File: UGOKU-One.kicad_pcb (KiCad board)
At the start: 2 copper layers, 70 x 70 mm, 80 parts, among them J1 ENC/IO, J10 Conn_01x02, J12 Conn_01x02, J2 SERVO, J3 Conn_02x03_Odd_Even, J4 14110213001000, J5 Conn_01x05, J6 Conn_01x02, J7 ENC/IO, J8 DAC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

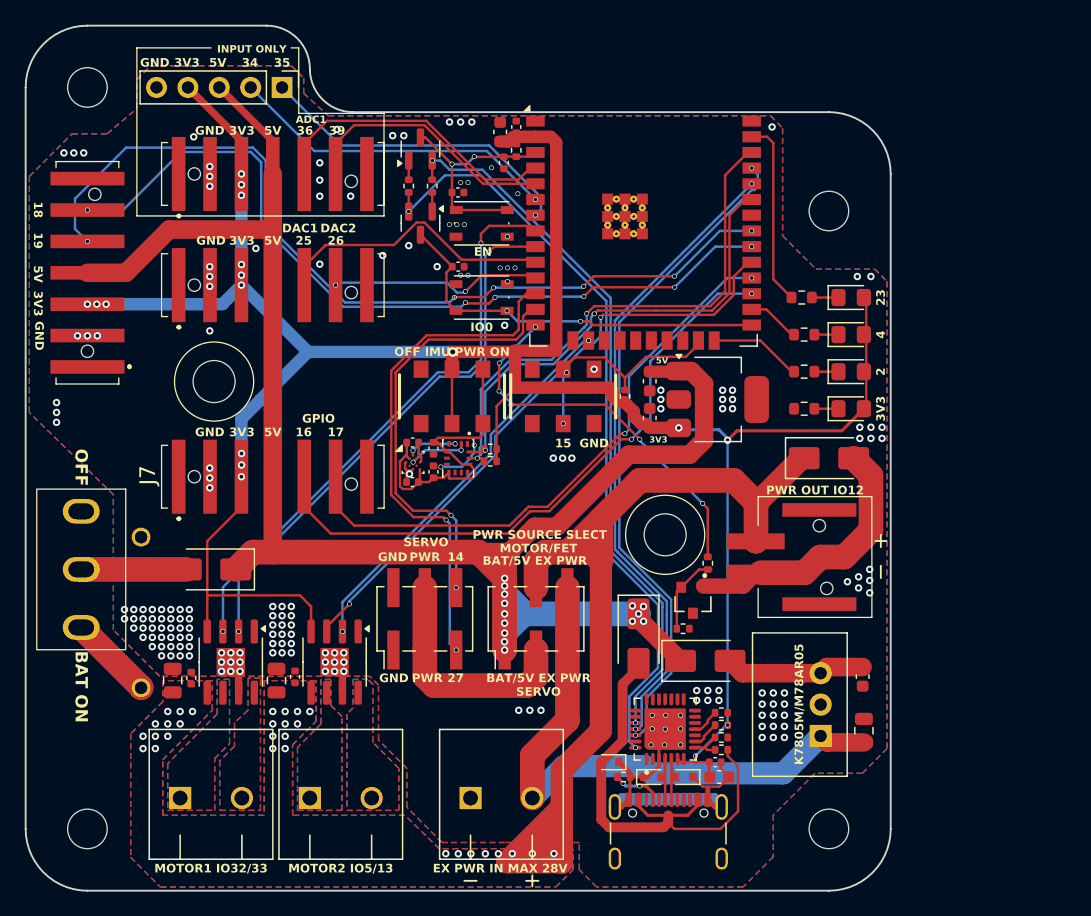
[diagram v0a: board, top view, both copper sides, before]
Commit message: correct TXRX, regulator pin assign add batt thermal pad
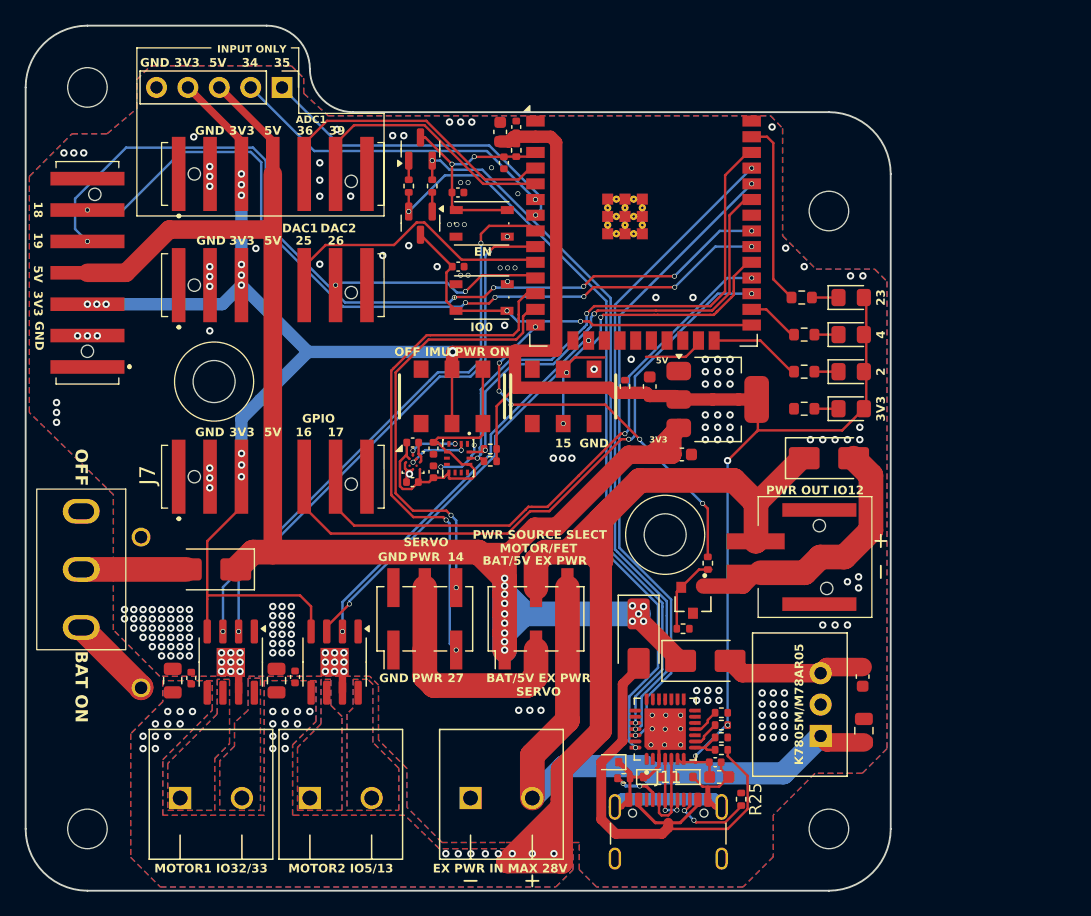
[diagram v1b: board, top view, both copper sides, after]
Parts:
- removed P1: USB_C_Plug_USB2.0, Connector_USB:USB_C_Receptacle_GCT_USB4105-xx-A_16P_TopMnt_Horizontal
- removed R17: 5.1k, Resistor_SMD:R_0402_1005Metric
- added J11: USB_C_Receptacle_USB2.0_16P, Connector_USB:USB_C_Receptacle_GCT_USB4105-xx-A_16P_TopMnt_Horizontal, F.Cu at (17.0, 31.3)
- added R20: 5.1k, Resistor_SMD:R_0402_1005Metric, F.Cu at (13.4, 25.9)
- added R25: 5.1k, Resistor_SMD:R_0402_1005Metric, F.Cu at (22.9, 27.6)
- moved C1 6.47 mm to (18.1, -0.30), turned to 0 degrees
- moved C10 2.55 mm to (15.5, -5.80)
- moved R22 0.80 mm to (13.5, -5.80)
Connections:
- U1 pad 1: 5V -> GND
- U1 pad 2: GND -> 3V3
- U1 pad 3: 3V3 -> 5V
- U2 pad 26: TXD -> RXD0
- U5 pad 34: RXD -> RXD0
- U5 pad 35: TXD -> RXD
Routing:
- net TXD: track 54.0 -> 0.00 mm, vias 2 -> 0
- net RXD0: track 0.00 -> 52.1 mm, vias 0 -> 2
- net 5V: track 146.4 -> 138.7 mm
- net Net-(J11-CC2): track 0.00 -> 6.71 mm, vias 0 -> 2
- net Slide_SW: track 18.7 -> 13.0 mm
- net Net-(P1-CC): track 4.00 -> 0.00 mm, vias 2 -> 0
- net Net-(J11-CC1): track 0.00 -> 4.00 mm, vias 0 -> 2
- net Net-(D3-A2): track 4.48 -> 7.73 mm
- net Net-(D4-A2): track 4.48 -> 7.22 mm, vias 0 -> 2
- net 3V3: track 204.5 -> 207.2 mm, vias 17 -> 16
- net USB_5V: track 38.8 -> 40.2 mm
- net RXD: track 51.6 -> 52.9 mm
- net GND: track 39.9 -> 40.0 mm, vias 188 -> 202
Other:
- board text added: "UGOKU One Ver1.0.1 UGOKU Lab 2025-5"
- board text removed: "UGOKU One Ver1.0.0 UGOKU Lab 2025-4"

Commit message: align resistor
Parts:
- moved R7 0.20 mm to (28.0, -13.0)
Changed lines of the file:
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@@
 	(footprint "Resistor_SMD:R_0603_1608Metric"
 		(layer "F.Cu")
-		(at 27.8 -13)
+		(at 28 -13)
 		(descr "Resistor SMD 0603 (1608 Metric), square (rectangular) end terminal, IPC_7351 nominal, (Body size source: IPC-SM-782 page 72, https://www.pcb-3d.com/wordpress/wp-content/uploads/ipc-sm-782a_amendment_1_and_2.pdf), generated with kicad-footprint-generator")
 		(tags "resistor")
@@
 	)
 	(gr_text "5V"
-		(at 16.5 -7.9 0)
+		(at 15.9 -2.4 0)
 		(layer "F.SilkS")
 		(effects
@@
 	)
 	(gr_text "3V3"
-		(at 16.2 -1.5 0)
+		(at 24.1 -7.4 0)
 		(layer "F.SilkS")
 		(effects

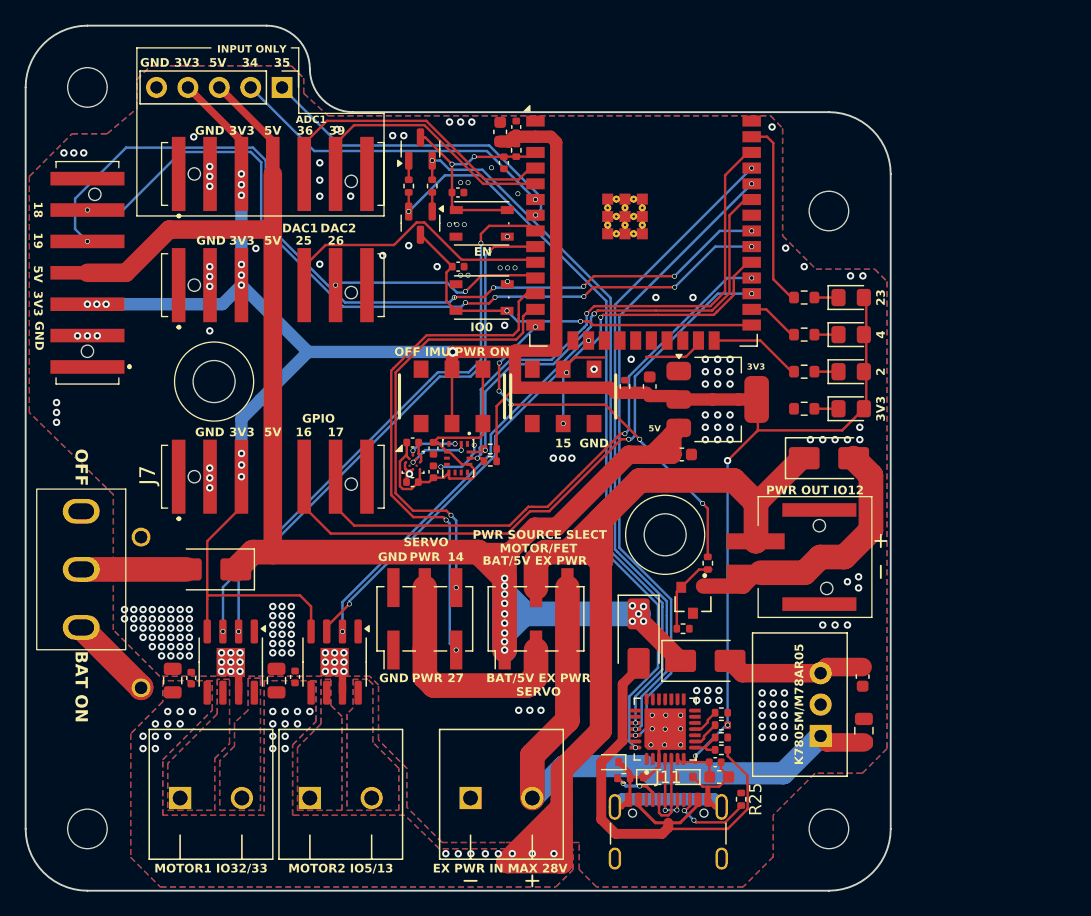
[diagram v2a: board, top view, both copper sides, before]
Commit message: add Motor Drive IN1/2 PIN PullDown, IO0 PIN PullUp
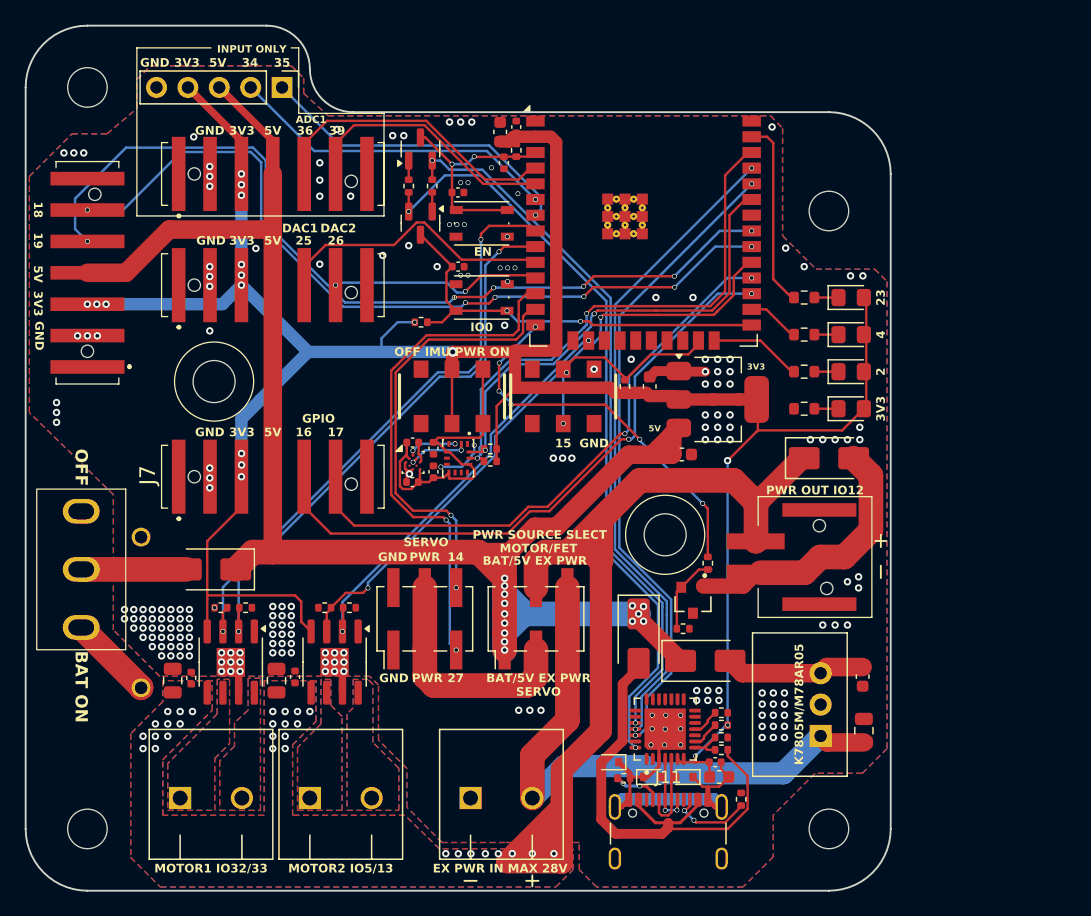
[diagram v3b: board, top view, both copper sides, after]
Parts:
- added R26: 10k, Resistor_SMD:R_0402_1005Metric, F.Cu at (-10.8, 12.1)
- added R29: 10k, Resistor_SMD:R_0402_1005Metric, F.Cu at (-8.80, 12.1)
- added R30: 10k, Resistor_SMD:R_0402_1005Metric, F.Cu at (-19.2, 12.1)
- added R31: 10k, Resistor_SMD:R_0402_1005Metric, F.Cu at (-17.2, 12.1)
- added R32: 10k, Resistor_SMD:R_0402_1005Metric, F.Cu at (-3.00, -11.0)
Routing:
- net Slide_SW: track 13.0 -> 17.9 mm
- net GND: track 40.0 -> 44.7 mm, vias 202 -> 203
- net 3V3: track 207.2 -> 211.3 mm, vias 16 -> 17
- net IO0: track 32.1 -> 34.8 mm
- net MD1_IN1: track 47.1 -> 49.2 mm
- net MD2_IN2: track 32.0 -> 33.9 mm
- net MD1_IN2: track 44.5 -> 46.0 mm
- net MD2_IN1: track 49.8 -> 50.6 mm
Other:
- board text added: "UGOKU One Ver1.1.0 UGOKU Lab 2025-6"
- board text removed: "UGOKU One Ver1.0.1 UGOKU Lab 2025-5"

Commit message: JLCPCBの要求に対応するため最小viaサイズを0.3/0.5に変更、JLCPCBの要求に対応するためvia-Padクリアランス確保のため地磁気センサBMM150を廃止、スイッチング出力用FETのピン配置を修正
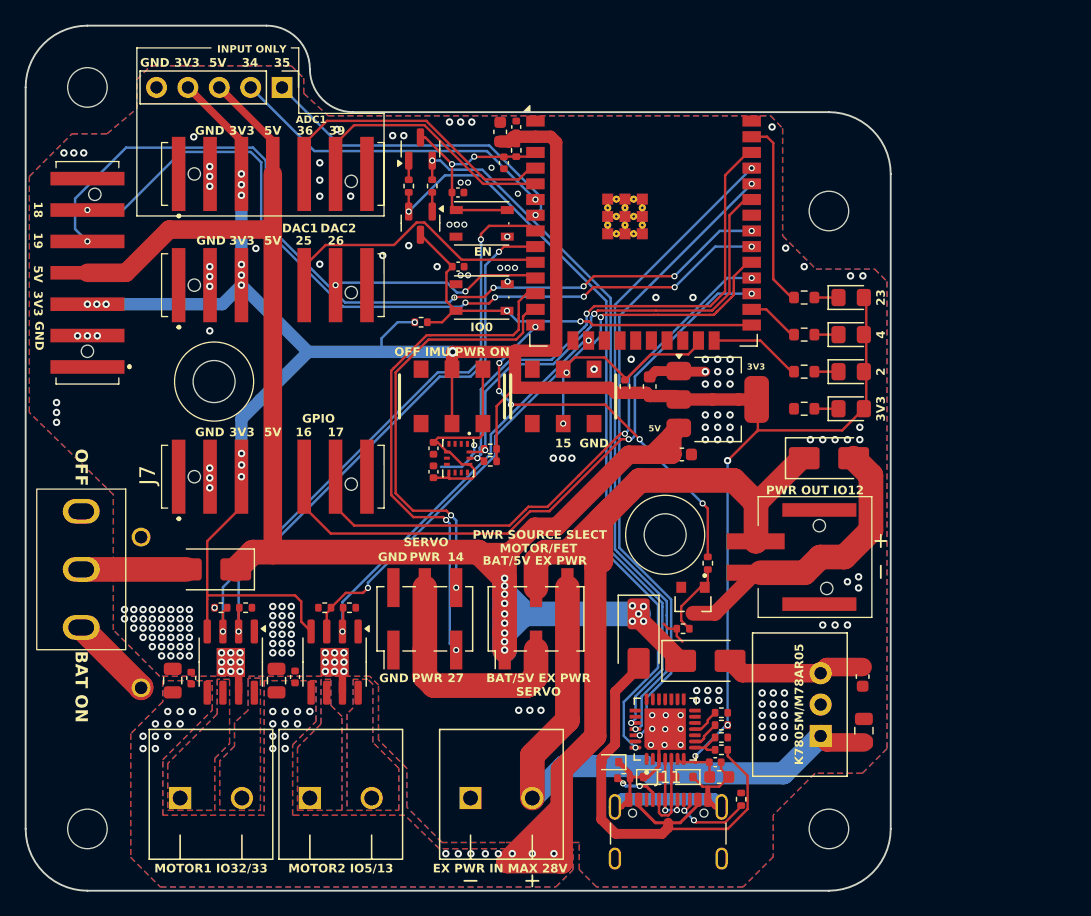
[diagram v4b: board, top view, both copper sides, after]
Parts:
- removed C13, C4: 0.1uF, Capacitor_SMD:C_0402_1005Metric
- removed U6: BMM150, Package_CSP:WLCSP-12_1.56x1.56mm_P0.4mm
- turned R23 to 180 degrees
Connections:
- Q1 pad 1: Net-(D8-A) -> Net-(Q1-G)
- Q1 pad 2: Net-(Q1-G) -> GND
- Q1 pad 3: GND -> Net-(D8-A)
- U7 pad 2: Net-(U6-SDI) -> unconnected-(U7-ASDX-Pad2)
- U7 pad 3: Net-(U6-SCK) -> unconnected-(U7-ASCX-Pad3)
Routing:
- net 3V3_IMU: track 26.9 -> 18.3 mm
- net Net-(U6-SDI): track 5.37 -> 0.00 mm, vias 2 -> 0
- net Net-(U6-SCK): track 4.02 -> 0.00 mm, vias 2 -> 0
- net Net-(D8-A): track 21.5 -> 23.2 mm
- net GND: track 44.7 -> 43.2 mm, vias 203 -> 200

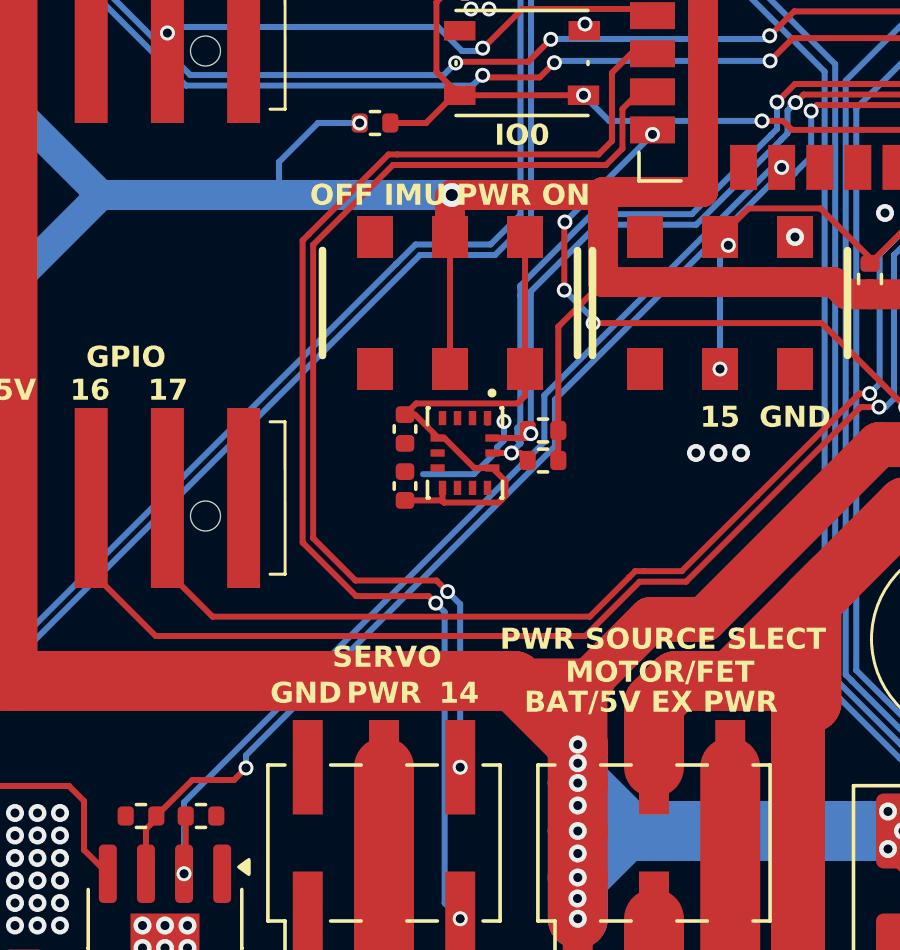
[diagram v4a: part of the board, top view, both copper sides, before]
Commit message: IMUの待機電力が微小のため、IMUの電源スイッチを廃止
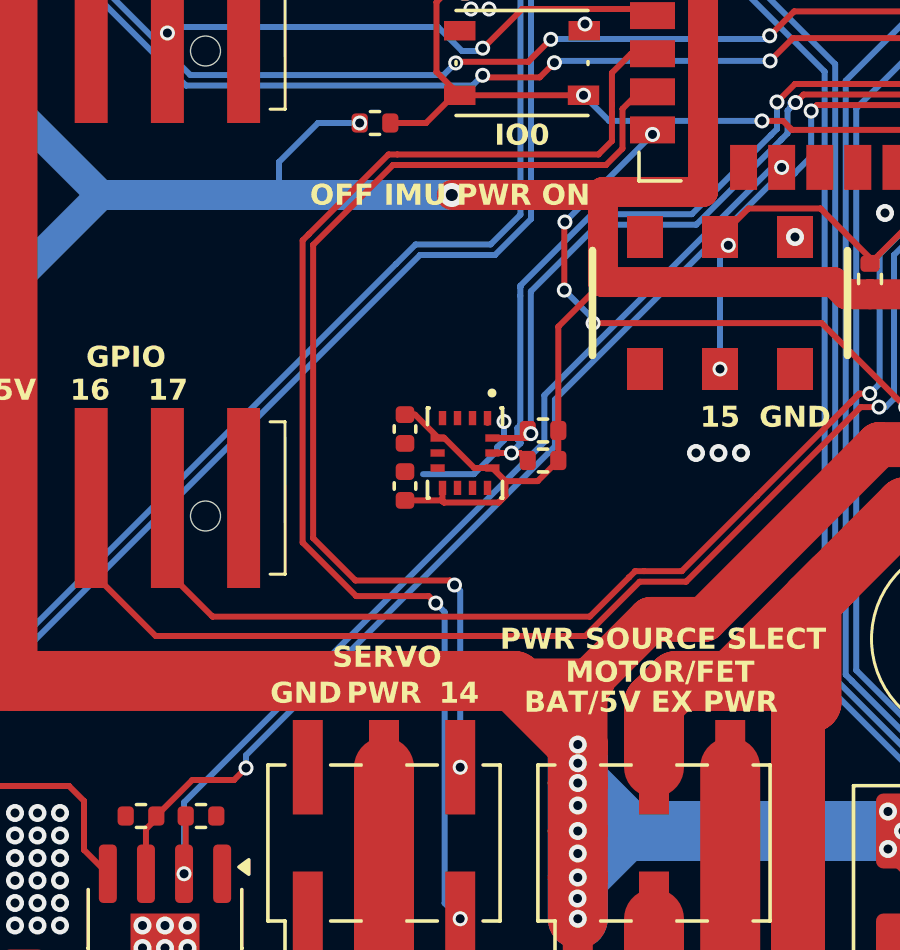
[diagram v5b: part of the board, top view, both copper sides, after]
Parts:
- removed SW5: SW_Slide_DPDT, 0_UGOKU-One_Lib:SSSS213202
- R13: value 2K -> 1.5k
- R4: value 510 -> 470
- R5, R6, R7: value 1k -> 1.5k
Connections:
- C14 pad 1: 3V3_IMU -> 3V3
- C15 pad 1: 3V3_IMU -> 3V3
- U7 pad 12: 3V3_IMU -> 3V3
- U7 pad 5: 3V3_IMU -> 3V3
- U7 pad 8: 3V3_IMU -> 3V3
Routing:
- net 3V3_IMU: track 18.3 -> 0.00 mm
- net 3V3: track 211.3 -> 216.3 mm
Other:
- board text added: "UGOKU One Ver1.1.1 UGOKU Lab 2025-6"
- board text removed: "UGOKU One Ver1.1.0 UGOKU Lab 2025-6"
